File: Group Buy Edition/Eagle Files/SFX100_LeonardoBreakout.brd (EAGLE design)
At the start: 130.8 x 55.9 mm, 6 parts, among them U1 ARDUINOR3-BPLACE

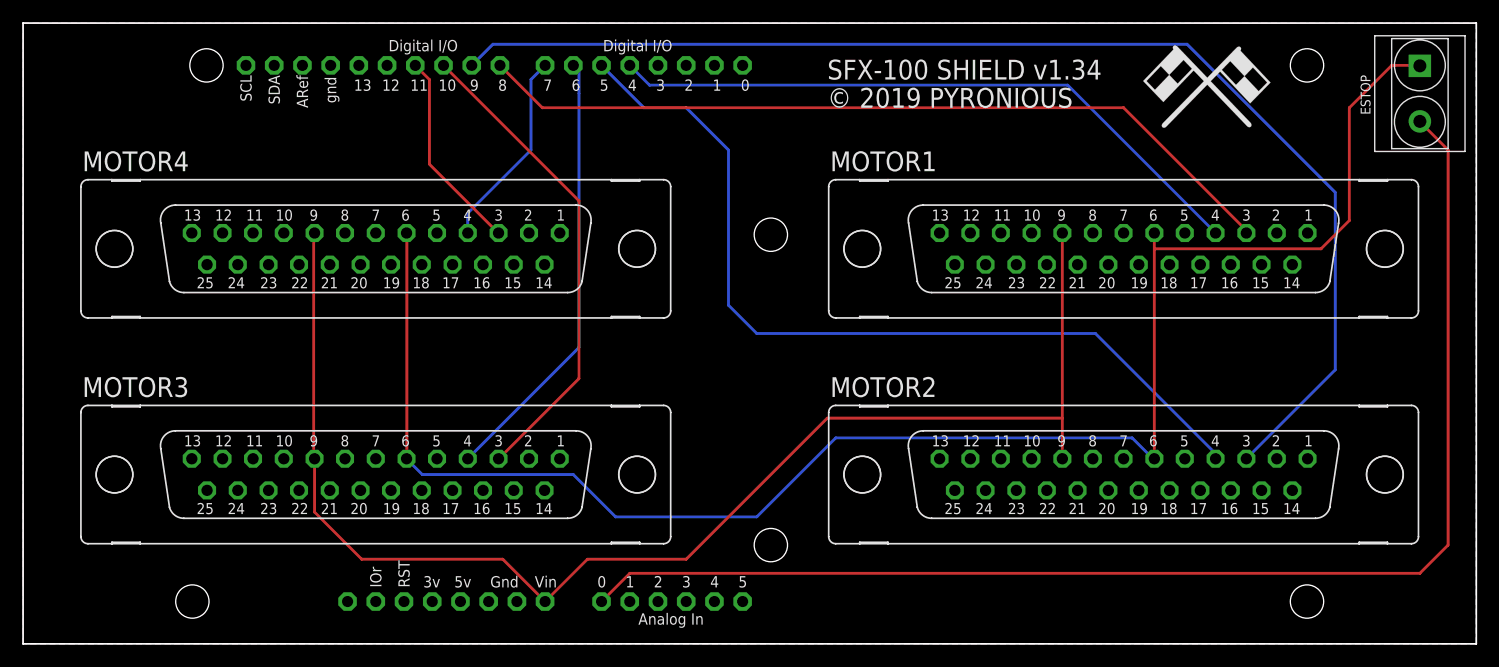
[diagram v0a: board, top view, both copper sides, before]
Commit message: Updated to final "group buy" design.
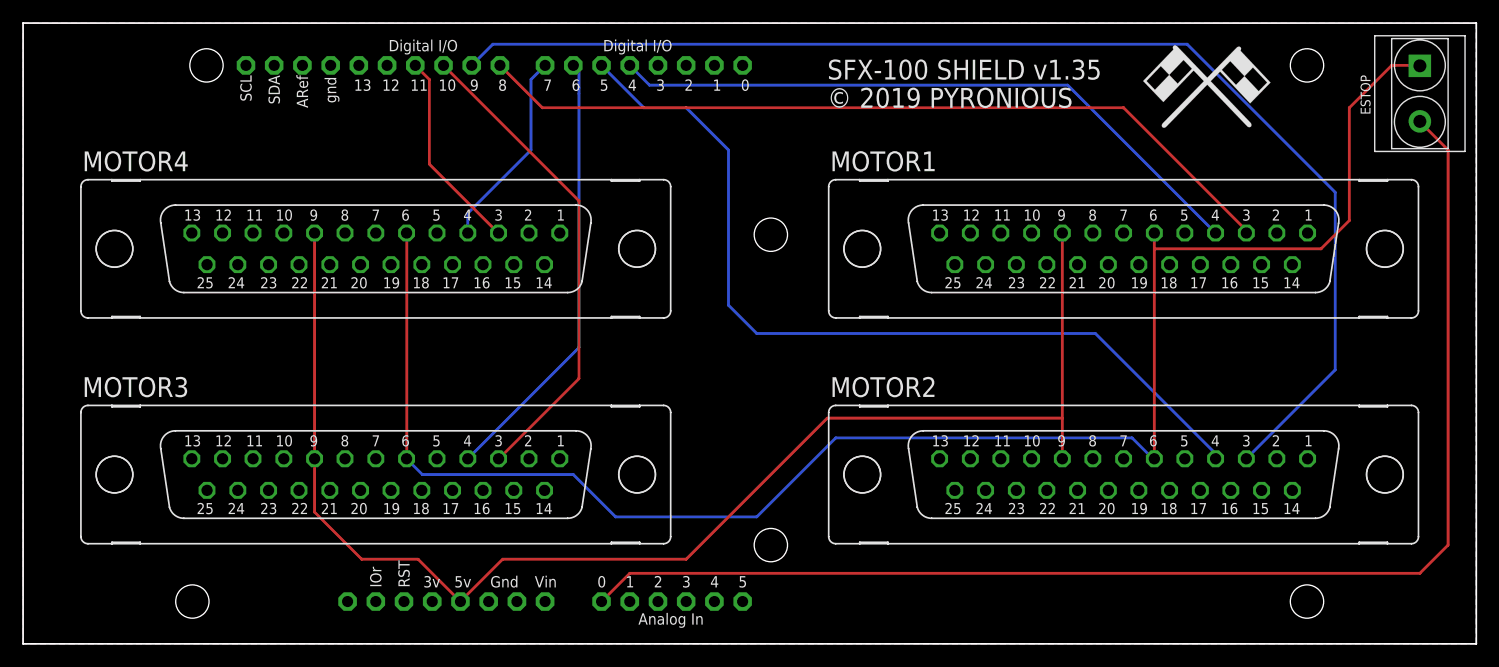
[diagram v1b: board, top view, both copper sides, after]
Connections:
- removed net VCC: MOTOR1.9, MOTOR2.9, MOTOR3.9, MOTOR4.9, U1.VIN
- new net VIN: U1.VIN
- net 5V: now also MOTOR1.9, MOTOR2.9, MOTOR3.9, MOTOR4.9
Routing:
- net VCC: track 123.0 -> 0.00 mm
- net 5V: track 0.00 -> 122.9 mm
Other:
- board text added: "SFX-100 SHIELD v1.35"
- board text removed: "SFX-100 SHIELD v1.34"
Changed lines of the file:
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@@
 <drawing>
 <settings>
-<setting alwaysvectorfont="yes"/>
+<setting alwaysvectorfont="no"/>
 <setting verticaltext="up"/>
 </settings>
@@
 <wire x1="129.54" y1="-1.27" x2="-1.27" y2="-1.27" width="0.1524" layer="20"/>
 <wire x1="-1.27" y1="-1.27" x2="-1.27" y2="54.61" width="0.1524" layer="20"/>
-<text x="71.12" y="49.53" size="1.778" layer="21" font="vector">SFX-100 SHIELD v1.34</text>
+<text x="71.12" y="49.53" size="1.778" layer="21" font="vector">SFX-100 SHIELD v1.35</text>
 <text x="71.12" y="46.99" size="1.778" layer="21" font="vector">© 2019 PYRONIOUS</text>
 <hole x="15.24" y="50.8" drill="3"/>
@@
 </class>
 </classes>
-<designrules name="SparkFun">
-<description language="en">&lt;b&gt;EAGLE Design Rules&lt;/b&gt;
+<designrules name="oshpark-2layer">
+<description language="en">&lt;b&gt;OSH Park Design Rules&lt;/b&gt;
 &lt;p&gt;
-The default Design Rules have been set to cover
-a wide range of applications. Your particular design
-may have different requirements, so please make the
-necessary adjustments and save your customized
-design rules under a new name.</description>
+Please make sure your boards conform to these design rules.
+&lt;/p&gt;
+&lt;p&gt;
+Note, that not all DRC settings must be set by the manufacturer. Several can be adjusted for the design, including those listed on our docs page here.
+&lt;a href=&quot;http://docs.oshpark.com/design-tools/eagle/design-rules-files/&quot;&gt;Adjustable Settings&lt;/a&gt;
+&lt;/p&gt;</description>
 <param name="layerSetup" value="(1*16)"/>
-<param name="mtCopper" value="0.035mm 0.035mm 0.035mm 0.035mm 0.035mm 0.035mm 0.035mm 0.035mm 0.035mm 0.035mm 0.035mm 0.035mm 0.035mm 0.035mm 0.035mm 0.035mm"/>
-<param name="mtIsolate" value="1.5mm 0.15mm 0.2mm 0.15mm 0.2mm 0.15mm 0.2mm 0.15mm 0.2mm 0.15mm 0.2mm 0.15mm 0.2mm 0.15mm 0.2mm"/>
-<param name="mdWireWire" value="8mil"/>
-<param name="mdWirePad" value="8mil"/>
-<param name="mdWireVia" value="8mil"/>
-<param name="mdPadPad" value="8mil"/>
-<param name="mdPadVia" value="8mil"/>
-<param name="mdViaVia" value="8mil"/>
-<param name="mdSmdPad" value="8mil"/>
-<param name="mdSmdVia" value="8mil"/>
-<param name="mdSmdSmd" value="8mil"/>
+<param name="mtCopper" value="0.035559375mm 0.0356mm 0.0356mm 0.0356mm 0.0356mm 0.0356mm 0.0356mm 0.0356mm 0.0356mm 0.0356mm 0.0356mm 0.0356mm 0.0356mm 0.0356mm 0.0356mm 0.035559375mm"/>
+<param name="mtIsolate" value="1.6mm 0.1499mm 0.2007mm 0.1499mm 0.2007mm 0.1499mm 0.2007mm 0.1499mm 0.2007mm 0.1499mm 0.2007mm 0.1499mm 0.2007mm 0.1499mm 0.2007mm"/>
+<param name="mdWireWire" value="6mil"/>
+<param name="mdWirePad" value="6mil"/>
+<param name="mdWireVia" value="6mil"/>
+<param name="mdPadPad" value="6mil"/>
+<param name="mdPadVia" value="6mil"/>
+<param name="mdViaVia" value="6mil"/>
+<param name="mdSmdPad" value="6mil"/>
+<param name="mdSmdVia" value="6mil"/>
+<param name="mdSmdSmd" value="6mil"/>
 <param name="mdViaViaSameLayer" value="8mil"/>
 <param name="mnLayersViaInSmd" value="2"/>
-<param name="mdCopperDimension" value="10mil"/>
-<param name="mdDrill" value="8mil"/>
+<param name="mdCopperDimension" value="15mil"/>
+<param name="mdDrill" value="6mil"/>
 <param name="mdSmdStop" value="0mil"/>
-<param name="msWidth" value="8mil"/>
-<param name="msDrill" value="20mil"/>
-<param name="msMicroVia" value="9.99mm"/>
+<param name="msWidth" value="6mil"/>
+<param name="msDrill" value="10mil"/>
+<param name="msMicroVia" value="10mil"/>
 <param name="msBlindViaRatio" value="0.5"/>
 <param name="rvPadTop" value="0.25"/>
@@
 <param name="rvMicroViaOuter" value="0.25"/>
 <param name="rvMicroViaInner" value="0.25"/>
-<param name="rlMinPadTop" value="12mil"/>
+<param name="rlMinPadTop" value="5mil"/>
 <param name="rlMaxPadTop" value="20mil"/>
-<param name="rlMinPadInner" value="10mil"/>
+<param name="rlMinPadInner" value="5mil"/>
 <param name="rlMaxPadInner" value="20mil"/>
-<param name="rlMinPadBottom" value="12mil"/>
+<param name="rlMinPadBottom" value="5mil"/>
 <param name="rlMaxPadBottom" value="20mil"/>
-<param name="rlMinViaOuter" value="10mil"/>
+<param name="rlMinViaOuter" value="5mil"/>
 <param name="rlMaxViaOuter" value="20mil"/>
-<param name="rlMinViaInner" value="10mil"/>
+<param name="rlMinViaInner" value="5mil"/>
 <param name="rlMaxViaInner" value="20mil"/>
-<param name="rlMinMicroViaOuter" value="4mil"/>
+<param name="rlMinMicroViaOuter" value="5mil"/>
 <param name="rlMaxMicroViaOuter" value="20mil"/>
-<param name="rlMinMicroViaInner" value="4mil"/>
+<param name="rlMinMicroViaInner" value="5mil"/>
 <param name="rlMaxMicroViaInner" value="20mil"/>
 <param name="psTop" value="-1"/>
@@
 <param name="mvStopFrame" value="1"/>
 <param name="mvCreamFrame" value="0"/>
-<param name="mlMinStopFrame" value="4mil"/>
-<param name="mlMaxStopFrame" value="4mil"/>
+<param name="mlMinStopFrame" value="2.5mil"/>
+<param name="mlMaxStopFrame" value="2.5mil"/>
 <param name="mlMinCreamFrame" value="0mil"/>
 <param name="mlMaxCreamFrame" value="0mil"/>
-<param name="mlViaStopLimit" value="25mil"/>
+<param name="mlViaStopLimit" value="0mil"/>
 <param name="srRoundness" value="0"/>
 <param name="srMinRoundness" value="0mil"/>
@@
 </polygon>
 </signal>
-<signal name="5V">
-<contactref element="U1" pad="5V"/>
-</signal>
 <signal name="3V">
 <contactref element="U1" pad="3V"/>
-</signal>
-<signal name="VCC">
-<contactref element="MOTOR3" pad="9"/>
-<contactref element="MOTOR2" pad="9"/>
-<contactref element="MOTOR1" pad="9"/>
-<contactref element="MOTOR4" pad="9"/>
-<contactref element="U1" pad="VIN"/>
-<wire x1="24.892" y1="15.494" x2="24.9682" y2="15.3924" width="0.254" layer="1"/>
-<wire x1="24.892" y1="35.56" x2="24.9682" y2="35.7124" width="0.254" layer="1"/>
-<wire x1="45.72" y1="2.54" x2="49.53" y2="6.35" width="0.254" layer="1"/>
-<wire x1="49.53" y1="6.35" x2="58.42" y2="6.35" width="0.254" layer="1"/>
-<wire x1="58.42" y1="6.35" x2="71.12" y2="19.05" width="0.254" layer="1"/>
-<wire x1="24.9682" y1="15.3924" x2="24.9682" y2="10.5918" width="0.254" layer="1"/>
-<wire x1="29.21" y1="6.35" x2="41.91" y2="6.35" width="0.254" layer="1"/>
-<wire x1="41.91" y1="6.35" x2="45.72" y2="2.54" width="0.254" layer="1"/>
-<wire x1="24.9682" y1="10.5918" x2="29.21" y2="6.35" width="0.254" layer="1"/>
-<wire x1="92.2782" y1="19.05" x2="92.2782" y2="35.7124" width="0.254" layer="1"/>
-<wire x1="24.892" y1="35.56" x2="24.892" y2="15.494" width="0.254" layer="1"/>
-<wire x1="71.12" y1="19.05" x2="92.2782" y2="19.05" width="0.254" layer="1"/>
-<wire x1="92.2782" y1="19.05" x2="92.2782" y2="15.3924" width="0.254" layer="1"/>
 </signal>
 <signal name="STEP4">
@@
 <wire x1="121.92" y1="50.8" x2="124.46" y2="50.8" width="0.254" layer="1"/>
 </signal>
+<signal name="VIN">
+<contactref element="U1" pad="VIN"/>
+</signal>
+<signal name="5V">
+<contactref element="U1" pad="5V"/>
+<contactref element="MOTOR3" pad="9"/>
+<contactref element="MOTOR2" pad="9"/>
+<contactref element="MOTOR1" pad="9"/>
+<wire x1="58.42" y1="6.35" x2="71.12" y2="19.05" width="0.254" layer="1"/>
+<wire x1="24.9682" y1="10.5918" x2="29.21" y2="6.35" width="0.254" layer="1"/>
+<wire x1="92.2782" y1="19.05" x2="92.2782" y2="35.7124" width="0.254" layer="1"/>
+<wire x1="71.12" y1="19.05" x2="92.2782" y2="19.05" width="0.254" layer="1"/>
+<wire x1="29.21" y1="6.35" x2="34.29" y2="6.35" width="0.254" layer="1"/>
+<contactref element="MOTOR4" pad="9"/>
+<wire x1="41.91" y1="6.35" x2="58.42" y2="6.35" width="0.254" layer="1"/>
+<wire x1="24.9682" y1="15.3924" x2="24.9682" y2="10.5918" width="0.254" layer="1"/>
+<wire x1="92.2782" y1="15.3924" x2="92.2782" y2="19.05" width="0.254" layer="1"/>
+<wire x1="24.9682" y1="35.7124" x2="24.9682" y2="15.3924" width="0.254" layer="1"/>
+<wire x1="38.1" y1="2.54" x2="34.29" y2="6.35" width="0.254" layer="1"/>
+<wire x1="38.1" y1="2.54" x2="41.91" y2="6.35" width="0.254" layer="1"/>
+</signal>
 </signals>
